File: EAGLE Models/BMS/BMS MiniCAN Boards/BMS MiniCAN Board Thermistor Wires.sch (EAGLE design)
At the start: 45 parts, among them IC1 AT90CAN128, IC2 MCP2551SO8, IC3 NUP2105L, IC5 FT232RL, Q1 56P2859, X2 6_PIN_CONNMOLEX_HORI, X3 6_PIN_CONNMOLEX_HORI, X4 6_PIN_CONNMOLEX_HORI, X5 6_PIN_CONNMOLEX_HORI, X6 6_PIN_CONNMOLEX_HORI

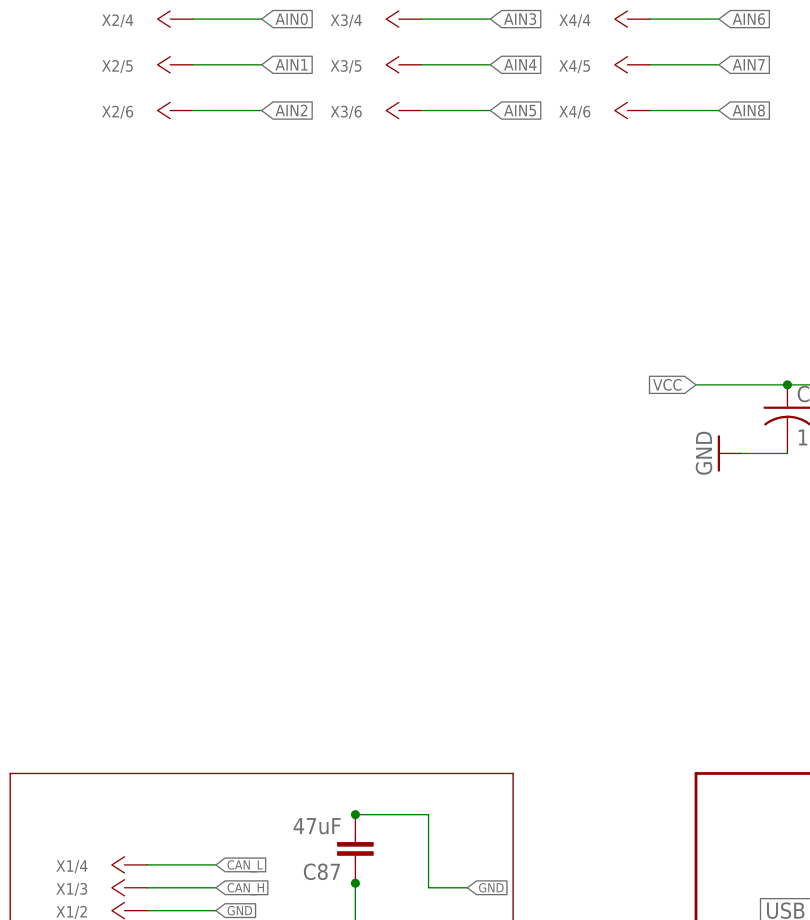
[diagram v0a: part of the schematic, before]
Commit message: added adc to lib
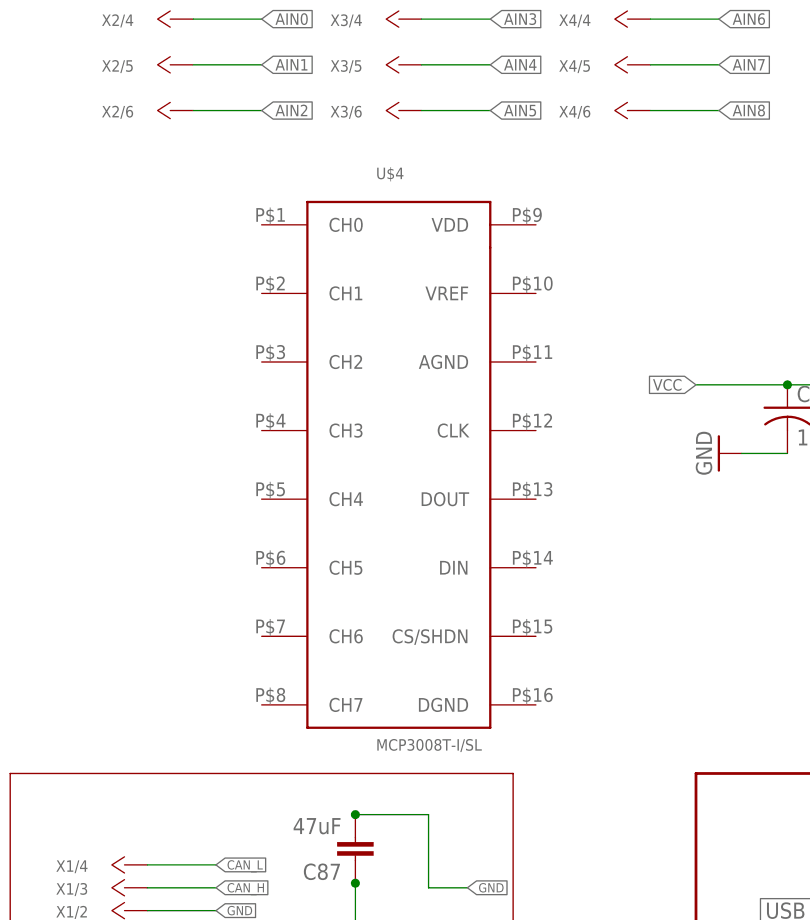
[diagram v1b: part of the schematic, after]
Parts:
- added U$3, U$4: MCP3008T-I/SL, BMS Lbr:MCP3008T-I/SL
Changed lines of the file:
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@@
 <grid distance="0.1" unitdist="inch" unit="inch" style="lines" multiple="1" display="no" altdistance="0.01" altunitdist="inch" altunit="inch"/>
 <layers>
-<layer number="1" name="Top" color="4" fill="1" visible="no" active="no"/>
-<layer number="2" name="Route2" color="1" fill="3" visible="no" active="no"/>
-<layer number="3" name="Route3" color="4" fill="3" visible="no" active="no"/>
-<layer number="14" name="Route14" color="1" fill="6" visible="no" active="no"/>
-<layer number="15" name="Route15" color="4" fill="6" visible="no" active="no"/>
-<layer number="16" name="Bottom" color="1" fill="1" visible="no" active="no"/>
-<layer number="17" name="Pads" color="2" fill="1" visible="no" active="no"/>
-<layer number="18" name="Vias" color="2" fill="1" visible="no" active="no"/>
-<layer number="19" name="Unrouted" color="6" fill="1" visible="no" active="no"/>
-<layer number="20" name="Dimension" color="15" fill="1" visible="no" active="no"/>
-<layer number="21" name="tPlace" color="7" fill="1" visible="no" active="no"/>
-<layer number="22" name="bPlace" color="7" fill="1" visible="no" active="no"/>
-<layer number="23" name="tOrigins" color="15" fill="1" visible="no" active="no"/>
-<layer number="24" name="bOrigins" color="15" fill="1" visible="no" active="no"/>
-<layer number="25" name="tNames" color="7" fill="1" visible="no" active="no"/>
-<layer number="26" name="bNames" color="7" fill="1" visible="no" active="no"/>
-<layer number="27" name="tValues" color="7" fill="1" visible="no" active="no"/>
-<layer number="28" name="bValues" color="7" fill="1" visible="no" active="no"/>
+<layer number="1" name="Top" color="4" fill="1" visible="yes" active="no"/>
+<layer number="2" name="Route2" color="1" fill="3" visible="yes" active="no"/>
+<layer number="3" name="Route3" color="4" fill="3" visible="yes" active="no"/>
+<layer number="14" name="Route14" color="1" fill="6" visible="yes" active="no"/>
+<layer number="15" name="Route15" color="4" fill="6" visible="yes" active="no"/>
+<layer number="16" name="Bottom" color="1" fill="1" visible="yes" active="no"/>
+<layer number="17" name="Pads" color="2" fill="1" visible="yes" active="no"/>
+<layer number="18" name="Vias" color="2" fill="1" visible="yes" active="no"/>
+<layer number="19" name="Unrouted" color="6" fill="1" visible="yes" active="no"/>
+<layer number="20" name="Dimension" color="15" fill="1" visible="yes" active="no"/>
+<layer number="21" name="tPlace" color="7" fill="1" visible="yes" active="no"/>
+<layer number="22" name="bPlace" color="7" fill="1" visible="yes" active="no"/>
+<layer number="23" name="tOrigins" color="15" fill="1" visible="yes" active="no"/>
+<layer number="24" name="bOrigins" color="15" fill="1" visible="yes" active="no"/>
+<layer number="25" name="tNames" color="7" fill="1" visible="yes" active="no"/>
+<layer number="26" name="bNames" color="7" fill="1" visible="yes" active="no"/>
+<layer number="27" name="tValues" color="7" fill="1" visible="yes" active="no"/>
+<layer number="28" name="bValues" color="7" fill="1" visible="yes" active="no"/>
 <layer number="29" name="tStop" color="7" fill="3" visible="no" active="no"/>
 <layer number="30" name="bStop" color="7" fill="6" visible="no" active="no"/>
@@
 <layer number="35" name="tGlue" color="7" fill="4" visible="no" active="no"/>
 <layer number="36" name="bGlue" color="7" fill="5" visible="no" active="no"/>
-<layer number="37" name="tTest" color="7" fill="1" visible="no" active="no"/>
-<layer number="38" name="bTest" color="7" fill="1" visible="no" active="no"/>
+<layer number="37" name="tTest" color="7" fill="1" visible="yes" active="no"/>
+<layer number="38" name="bTest" color="7" fill="1" visible="yes" active="no"/>
 <layer number="39" name="tKeepout" color="4" fill="11" visible="no" active="no"/>
 <layer number="40" name="bKeepout" color="1" fill="11" visible="no" active="no"/>
@@
 <layer number="44" name="Drills" color="7" fill="1" visible="no" active="no"/>
 <layer number="45" name="Holes" color="7" fill="1" visible="no" active="no"/>
-<layer number="46" name="Milling" color="3" fill="1" visible="no" active="no"/>
-<layer number="47" name="Measures" color="7" fill="1" visible="no" active="no"/>
-<layer number="48" name="Document" color="7" fill="1" visible="no" active="no"/>
-<layer number="49" name="Reference" color="7" fill="1" visible="no" active="no"/>
-<layer number="50" name="dxf" color="7" fill="1" visible="no" active="no"/>
-<layer number="51" name="tDocu" color="7" fill="1" visible="no" active="no"/>
-<layer number="52" name="bDocu" color="7" fill="1" visible="no" active="no"/>
-<layer number="53" name="tGND_GNDA" color="7" fill="9" visible="no" active="no"/>
-<layer number="54" name="bGND_GNDA" color="1" fill="9" visible="no" active="no"/>
-<layer number="56" name="wert" color="7" fill="1" visible="no" active="no"/>
-<layer number="57" name="tCAD" color="7" fill="1" visible="no" active="no"/>
+<layer number="46" name="Milling" color="3" fill="1" visible="yes" active="no"/>
+<layer number="47" name="Measures" color="7" fill="1" visible="yes" active="no"/>
+<layer number="48" name="Document" color="7" fill="1" visible="yes" active="no"/>
+<layer number="49" name="Reference" color="7" fill="1" visible="yes" active="no"/>
+<layer number="50" name="dxf" color="7" fill="1" visible="yes" active="no"/>
+<layer number="51" name="tDocu" color="7" fill="1" visible="yes" active="no"/>
+<layer number="52" name="bDocu" color="7" fill="1" visible="yes" active="no"/>
+<layer number="53" name="tGND_GNDA" color="7" fill="9" visible="yes" active="no"/>
+<layer number="54" name="bGND_GNDA" color="1" fill="9" visible="yes" active="no"/>
+<layer number="56" name="wert" color="7" fill="1" visible="yes" active="no"/>
+<layer number="57" name="tCAD" color="7" fill="1" visible="yes" active="no"/>
 <layer number="90" name="Modules" color="5" fill="1" visible="yes" active="yes"/>
 <layer number="91" name="Nets" color="2" fill="1" visible="yes" active="yes"/>
@@
 <part name="U$1" library="BMS Lbr" deviceset="LM117MPX-5.0" device=""/>
 <part name="C3" library="resistor" deviceset="C-US" device="C0805" value="10uF"/>
+<part name="U$3" library="BMS Lbr" deviceset="MCP3008T-I/SL" device=""/>
+<part name="U$4" library="BMS Lbr" deviceset="MCP3008T-I/SL" device=""/>
 </parts>
 <sheets>
@@
 <instance part="U$1" gate="G$1" x="231.14" y="177.8"/>
 <instance part="C3" gate="G$1" x="248.92" y="177.8"/>
+<instance part="U$4" gate="G$1" x="27.94" y="119.38"/>
 </instances>
 <busses>

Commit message: Fixed new adc
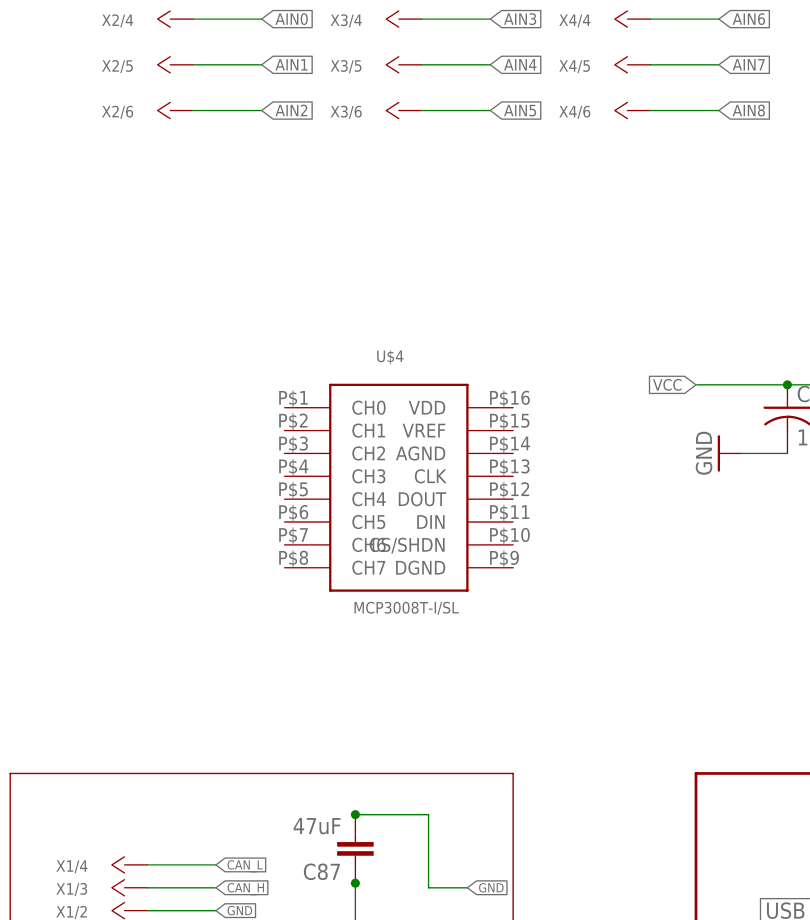
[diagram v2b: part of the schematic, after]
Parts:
- removed U$3: MCP3008T-I/SL, BMS Lbr:MCP3008T-I/SL
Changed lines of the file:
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@@
 <grid distance="0.1" unitdist="inch" unit="inch" style="lines" multiple="1" display="no" altdistance="0.01" altunitdist="inch" altunit="inch"/>
 <layers>
-<layer number="1" name="Top" color="4" fill="1" visible="yes" active="no"/>
-<layer number="2" name="Route2" color="1" fill="3" visible="yes" active="no"/>
-<layer number="3" name="Route3" color="4" fill="3" visible="yes" active="no"/>
-<layer number="14" name="Route14" color="1" fill="6" visible="yes" active="no"/>
-<layer number="15" name="Route15" color="4" fill="6" visible="yes" active="no"/>
-<layer number="16" name="Bottom" color="1" fill="1" visible="yes" active="no"/>
-<layer number="17" name="Pads" color="2" fill="1" visible="yes" active="no"/>
-<layer number="18" name="Vias" color="2" fill="1" visible="yes" active="no"/>
-<layer number="19" name="Unrouted" color="6" fill="1" visible="yes" active="no"/>
-<layer number="20" name="Dimension" color="15" fill="1" visible="yes" active="no"/>
-<layer number="21" name="tPlace" color="7" fill="1" visible="yes" active="no"/>
-<layer number="22" name="bPlace" color="7" fill="1" visible="yes" active="no"/>
-<layer number="23" name="tOrigins" color="15" fill="1" visible="yes" active="no"/>
-<layer number="24" name="bOrigins" color="15" fill="1" visible="yes" active="no"/>
-<layer number="25" name="tNames" color="7" fill="1" visible="yes" active="no"/>
-<layer number="26" name="bNames" color="7" fill="1" visible="yes" active="no"/>
-<layer number="27" name="tValues" color="7" fill="1" visible="yes" active="no"/>
-<layer number="28" name="bValues" color="7" fill="1" visible="yes" active="no"/>
+<layer number="1" name="Top" color="4" fill="1" visible="no" active="no"/>
+<layer number="2" name="Route2" color="1" fill="3" visible="no" active="no"/>
+<layer number="3" name="Route3" color="4" fill="3" visible="no" active="no"/>
+<layer number="14" name="Route14" color="1" fill="6" visible="no" active="no"/>
+<layer number="15" name="Route15" color="4" fill="6" visible="no" active="no"/>
+<layer number="16" name="Bottom" color="1" fill="1" visible="no" active="no"/>
+<layer number="17" name="Pads" color="2" fill="1" visible="no" active="no"/>
+<layer number="18" name="Vias" color="2" fill="1" visible="no" active="no"/>
+<layer number="19" name="Unrouted" color="6" fill="1" visible="no" active="no"/>
+<layer number="20" name="Dimension" color="15" fill="1" visible="no" active="no"/>
+<layer number="21" name="tPlace" color="7" fill="1" visible="no" active="no"/>
+<layer number="22" name="bPlace" color="7" fill="1" visible="no" active="no"/>
+<layer number="23" name="tOrigins" color="15" fill="1" visible="no" active="no"/>
+<layer number="24" name="bOrigins" color="15" fill="1" visible="no" active="no"/>
+<layer number="25" name="tNames" color="7" fill="1" visible="no" active="no"/>
+<layer number="26" name="bNames" color="7" fill="1" visible="no" active="no"/>
+<layer number="27" name="tValues" color="7" fill="1" visible="no" active="no"/>
+<layer number="28" name="bValues" color="7" fill="1" visible="no" active="no"/>
 <layer number="29" name="tStop" color="7" fill="3" visible="no" active="no"/>
 <layer number="30" name="bStop" color="7" fill="6" visible="no" active="no"/>
@@
 <layer number="35" name="tGlue" color="7" fill="4" visible="no" active="no"/>
 <layer number="36" name="bGlue" color="7" fill="5" visible="no" active="no"/>
-<layer number="37" name="tTest" color="7" fill="1" visible="yes" active="no"/>
-<layer number="38" name="bTest" color="7" fill="1" visible="yes" active="no"/>
+<layer number="37" name="tTest" color="7" fill="1" visible="no" active="no"/>
+<layer number="38" name="bTest" color="7" fill="1" visible="no" active="no"/>
 <layer number="39" name="tKeepout" color="4" fill="11" visible="no" active="no"/>
 <layer number="40" name="bKeepout" color="1" fill="11" visible="no" active="no"/>
@@
 <layer number="44" name="Drills" color="7" fill="1" visible="no" active="no"/>
 <layer number="45" name="Holes" color="7" fill="1" visible="no" active="no"/>
-<layer number="46" name="Milling" color="3" fill="1" visible="yes" active="no"/>
-<layer number="47" name="Measures" color="7" fill="1" visible="yes" active="no"/>
-<layer number="48" name="Document" color="7" fill="1" visible="yes" active="no"/>
-<layer number="49" name="Reference" color="7" fill="1" visible="yes" active="no"/>
-<layer number="50" name="dxf" color="7" fill="1" visible="yes" active="no"/>
-<layer number="51" name="tDocu" color="7" fill="1" visible="yes" active="no"/>
-<layer number="52" name="bDocu" color="7" fill="1" visible="yes" active="no"/>
-<layer number="53" name="tGND_GNDA" color="7" fill="9" visible="yes" active="no"/>
-<layer number="54" name="bGND_GNDA" color="1" fill="9" visible="yes" active="no"/>
-<layer number="56" name="wert" color="7" fill="1" visible="yes" active="no"/>
-<layer number="57" name="tCAD" color="7" fill="1" visible="yes" active="no"/>
+<layer number="46" name="Milling" color="3" fill="1" visible="no" active="no"/>
+<layer number="47" name="Measures" color="7" fill="1" visible="no" active="no"/>
+<layer number="48" name="Document" color="7" fill="1" visible="no" active="no"/>
+<layer number="49" name="Reference" color="7" fill="1" visible="no" active="no"/>
+<layer number="50" name="dxf" color="7" fill="1" visible="no" active="no"/>
+<layer number="51" name="tDocu" color="7" fill="1" visible="no" active="no"/>
+<layer number="52" name="bDocu" color="7" fill="1" visible="no" active="no"/>
+<layer number="53" name="tGND_GNDA" color="7" fill="9" visible="no" active="no"/>
+<layer number="54" name="bGND_GNDA" color="1" fill="9" visible="no" active="no"/>
+<layer number="56" name="wert" color="7" fill="1" visible="no" active="no"/>
+<layer number="57" name="tCAD" color="7" fill="1" visible="no" active="no"/>
 <layer number="90" name="Modules" color="5" fill="1" visible="yes" active="yes"/>
 <layer number="91" name="Nets" color="2" fill="1" visible="yes" active="yes"/>
@@
 <part name="U$1" library="BMS Lbr" deviceset="LM117MPX-5.0" device=""/>
 <part name="C3" library="resistor" deviceset="C-US" device="C0805" value="10uF"/>
-<part name="U$3" library="BMS Lbr" deviceset="MCP3008T-I/SL" device=""/>
 <part name="U$4" library="BMS Lbr" deviceset="MCP3008T-I/SL" device=""/>
 </parts>

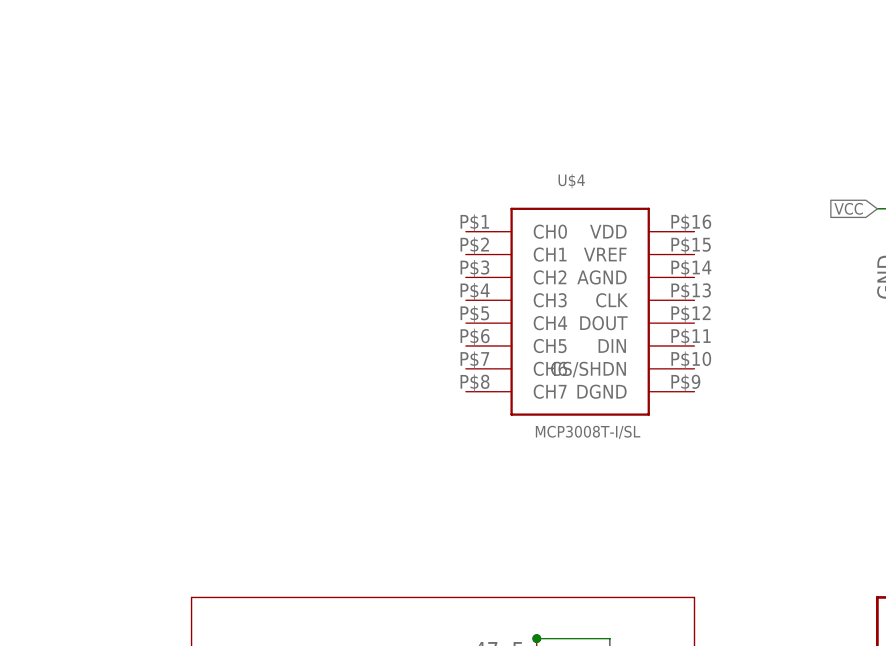
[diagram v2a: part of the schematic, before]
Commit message: Fixed Multiplexer symbol
Multiplexer symbol was off the center, recentered it. Added a
multiplexer to the thermistor wires schematic. Will add more
multiplexers.
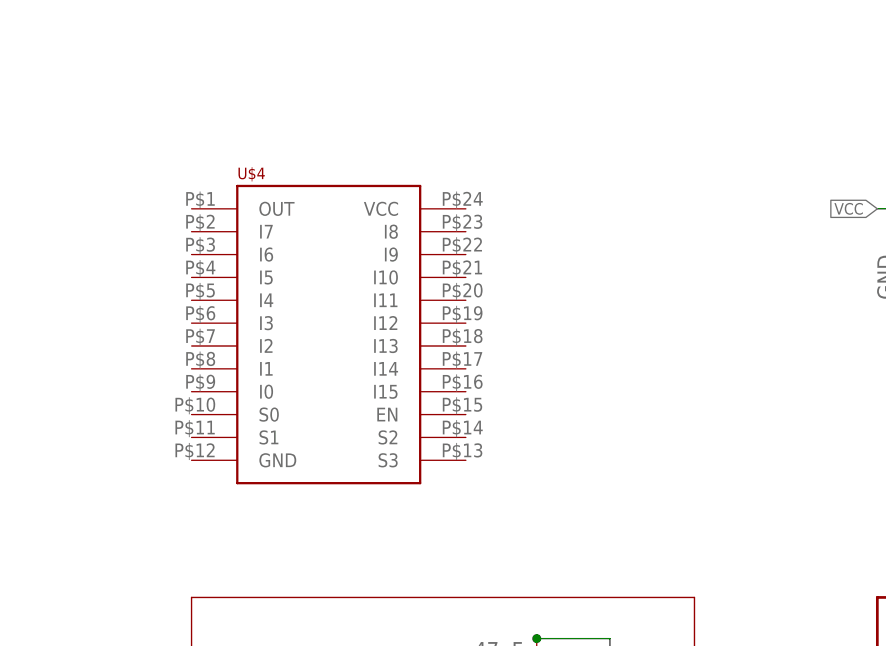
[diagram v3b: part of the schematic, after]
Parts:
- U$4: value MCP3008T-I/SL -> CD74HC4067; device BMS Lbr:MCP3008T-I/SL -> BMS Lbr:CD74HC4067
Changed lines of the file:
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@@
 <part name="U$1" library="BMS Lbr" deviceset="LM117MPX-5.0" device=""/>
 <part name="C3" library="resistor" deviceset="C-US" device="C0805" value="10uF"/>
-<part name="U$4" library="BMS Lbr" deviceset="MCP3008T-I/SL" device=""/>
+<part name="U$4" library="BMS Lbr" deviceset="CD74HC4067" device=""/>
 </parts>
 <sheets>
@@
 <instance part="U$1" gate="G$1" x="231.14" y="177.8"/>
 <instance part="C3" gate="G$1" x="248.92" y="177.8"/>
-<instance part="U$4" gate="G$1" x="27.94" y="119.38"/>
+<instance part="U$4" gate="G$1" x="0" y="116.84"/>
 </instances>
 <busses>
